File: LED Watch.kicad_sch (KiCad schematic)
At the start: 0 parts

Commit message: first schematic progress commit. adding RGB sketch schematic as well as completed single LED ring sketch. need to add buttons and sort out AND gates in the RGB sketch.
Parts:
- added D1, D10, D100, D101, D102, D103, D104, D105, D106, D107, D108, D109, D11, D110, D111, D112, D113, D114, D115, D116, D117, D118, D119, D12, D120, D121, D122, D123, D124, D125, D126, D127, D128, D129, D13, D130, D131, D132, D14, D15, D16, D17, D18, D19, D2, D20, D21, D22, D23, D24, D25, D26, D27, D28, D29, D3, D30, D31, D32, D33, D34, D35, D36, D37, D38, D39, D4, D40, D41, D42, D43, D44, D45, D46, D47, D48, D49, D5, D50, D51, D52, D53, D54, D55, D56, D57, D58, D59, D6, D60, D61, D62, D63, D64, D65, D66, D67, D68, D69, D7, D70, D71, D72, D73, D74, D75, D76, D77, D78, D79, D8, D80, D81, D82, D83, D84, D85, D86, D87, D88, D89, D9, D90, D91, D92, D93, D94, D95, D96, D97, D98, D99: LG_L29K-G2J1-24-Z, digikey-footprints:0603, symbol dk_LED-Indication-Discrete:LG_L29K-G2J1-24-Z
- added Q1, Q10, Q11, Q12, Q13, Q2, Q3, Q4, Q5, Q6, Q7, Q8, Q9: BD135, Package_TO_SOT_THT:TO-126-3_Vertical, symbol Transistor_BJT:BD135
- added R1, R10, R11, R12, R13, R14, R15, R16, R17, R18, R19, R2, R20, R21, R22, R23, R24, R25, R3, R4, R5, R6, R7, R8, R9: R_US, symbol Device:R_US
- added U1: ATMEGA32U4-AU, digikey-footprints:TQFP-44_10x10mm, symbol dk_Embedded-Microcontrollers:ATMEGA32U4-AU
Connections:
- new net: D51.2, D60.2, D61.1, D70.1, Q6.2 (C)
- new net: D61.2, D70.2, D71.1, D80.1, Q7.2 (C)
- new net: D32.2, D42.1
- new net: D42.2, D52.1
- new net: D121.2, D122.2, D123.2, D124.2, D125.2, D126.2, D127.2, D128.2, D129.2, D130.2, D131.2, D132.2, Q13.2 (C)
- new net: Q13.3 (B), R1.2
- new net: Q8.3 (B), R6.2
- new net: D1.2, D10.2, D11.1, D20.1, Q1.2 (C)
- new net: D11.2, D20.2, D21.1, D30.1, Q2.2 (C)
- new net: D18.1, D8.2
- new net: D18.2, D28.1
- new net: D41.2, D50.2, D51.1, D60.1, Q5.2 (C)
- new net: Q5.3 (B), R9.2
- new net: Q7.3 (B), R7.2
- new net: D109.1, D99.2
- new net: D109.2, D119.1
- new net: D105.1, D95.2
- new net: D105.2, D115.1
- new net: D100.1, D81.2, D90.2, D91.1, Q9.2 (C)
- new net: D100.2, D101.1, D110.1, D91.2, Q10.2 (C)
- new net: D83.2, D93.1
- new net: D103.1, D93.2
- new net: D112.2, D122.1
- new net: D117.2, D127.1
- new net: D9.1, R22.2
- new net: D74.2, D84.1
- new net: D84.2, D94.1
- new net: D103.2, D113.1
- new net: D113.2, D123.1
- new net: D21.2, D30.2, D31.1, D40.1, Q3.2 (C)
- new net: D53.2, D63.1
- new net: D63.2, D73.1
- new net: D10.1, R23.2
- new net: D31.2, D40.2, D41.1, D50.1, Q4.2 (C)
- new net: D16.1, D6.2
- new net: D16.2, D26.1
- new net: D78.2, D88.1
- new net: D88.2, D98.1
- new net: D108.2, D118.1
- new net: D118.2, D128.1
- new net: D37.2, D47.1
- new net: D47.2, D57.1
- new net: D14.1, D4.2
- new net: D14.2, D24.1
- new net: D102.1, D92.2
- new net: D102.2, D112.1
- new net: D71.2, D80.2, D81.1, D90.1, Q8.2 (C)
- new net: D39.2, D49.1
- new net: D49.2, D59.1
- new net: D15.1, D5.2
- new net: D15.2, D25.1
- new net: D54.2, D64.1
- new net: D64.2, D74.1
- new net: D116.2, D126.1
- new net: D17.1, D7.2
- new net: D17.2, D27.1
- new net: D48.2, D58.1
- new net: D58.2, D68.1
- new net: D5.1, R18.2
- new net: Q2.3 (B), R12.2
- new net: Q3.3 (B), R11.2
- new net: D19.1, D9.2
- new net: D19.2, D29.1
- new net: D67.2, D77.1
- new net: D77.2, D87.1
- new net: D132.1, D7.1, R20.2, R25.2
- new net: D27.2, D37.1
- new net: D8.1, R21.2
- new net: D57.2, D67.1
- new net: D101.2, D110.2, D111.1, D120.1, Q11.2 (C)
- new net: Q11.3 (B), R3.2
- new net: D2.1, R15.2
- new net: D12.1, D2.2
- new net: D87.2, D97.1
- new net: D107.1, D97.2
- new net: D29.2, D39.1
- new net: D62.2, D72.1
- new net: D72.2, D82.1
- new net: D66.2, D76.1
- new net: D76.2, D86.1
- new net: D69.2, D79.1
- new net: D79.2, D89.1
- new net: D131.1, D6.1, R19.2, R24.2
- new net: D86.2, D96.1
- new net: D106.2, D116.1
- new net: Q6.3 (B), R8.2
- new net: D65.2, D75.1
- new net: D75.2, D85.1
- new net: D46.2, D56.1
- new net: D56.2, D66.1
- new net: D45.2, D55.1
- new net: D55.2, D65.1
- new net: Q9.3 (B), R5.2
- new net: D107.2, D117.1
- new net: D52.2, D62.1
- new net: D4.1, R17.2
- new net: D111.2, D120.2, D121.1, D130.1, Q12.2 (C)
- new net: D119.2, D129.1
- new net: D13.1, D3.2
- new net: D13.2, D23.1
- new net: Q1.3 (B), R13.2
- new net: Q10.3 (B), R4.2
- new net: Q4.3 (B), R10.2
- new net: Q12.3 (B), R2.2
- new net: D89.2, D99.1
- new net: D22.2, D32.1
- new net: D114.2, D124.1
- new net: D25.2, D35.1
- new net: D108.1, D98.2
- new net: D34.2, D44.1
- new net: D44.2, D54.1
- new net: D68.2, D78.1
- new net: D106.1, D96.2
- new net: D23.2, D33.1
- new net: D33.2, D43.1
- new net: D85.2, D95.1
- new net: D12.2, D22.1
- new net: D73.2, D83.1
- new net: D59.2, D69.1
- new net: D82.2, D92.1
- new net: D115.2, D125.1
- new net: D1.1, R14.2
- new net: D3.1, R16.2
- new net: D104.1, D94.2
- new net: D104.2, D114.1
- new net: D26.2, D36.1
- new net: D36.2, D46.1
- new net: D35.2, D45.1
- new net: D28.2, D38.1
- new net: D38.2, D48.1
- new net: D43.2, D53.1
- new net: D24.2, D34.1
- new net GND: Q1.1 (E), Q10.1 (E), Q11.1 (E), Q12.1 (E), Q13.1 (E), Q2.1 (E), Q3.1 (E), Q4.1 (E), Q5.1 (E), Q6.1 (E), Q7.1 (E), Q8.1 (E), Q9.1 (E)

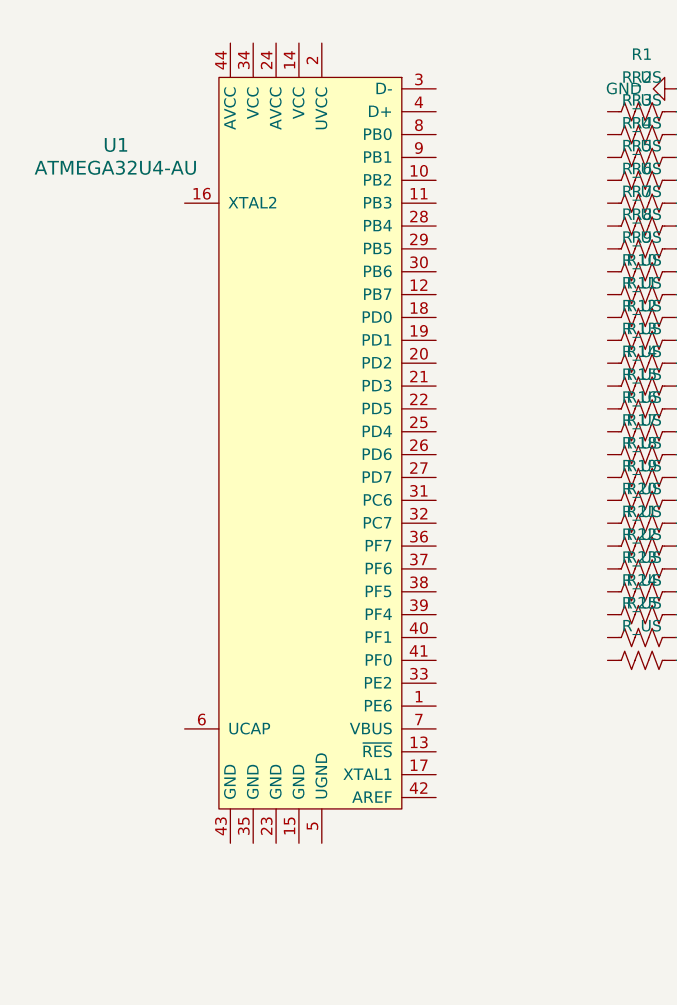
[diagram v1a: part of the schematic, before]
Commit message: chip swap to atmega4808
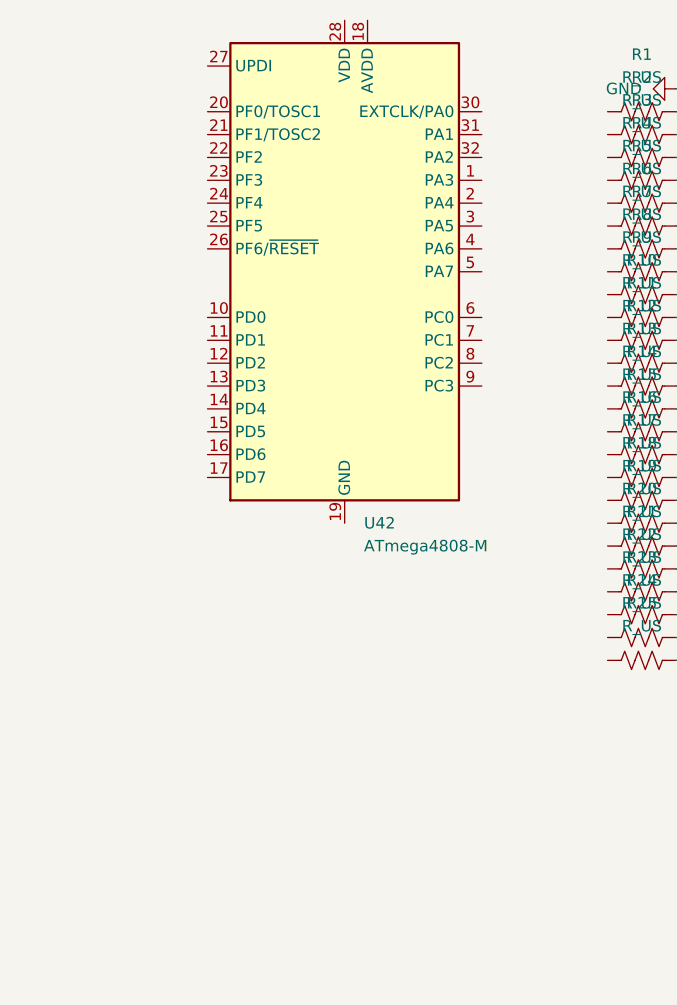
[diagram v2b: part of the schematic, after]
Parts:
- removed U1: ATMEGA32U4-AU, digikey-footprints:TQFP-44_10x10mm, symbol dk_Embedded-Microcontrollers:ATMEGA32U4-AU
- added U42: ATmega4808-M, Package_DFN_QFN:QFN-32-1EP_5x5mm_P0.5mm_EP3.1x3.1mm_ThermalVias, symbol MCU_Microchip_ATmega:ATmega4808-M
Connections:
- new net: U42.19 (GND), U42.29 (GND), U42.33 (GND)
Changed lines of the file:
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@@
 	)
 	(symbol
-		(lib_id "dk_Embedded-Microcontrollers:ATMEGA32U4-AU")
-		(at 110.49 102.87 0)
-		(mirror y)
-		(unit 1)
-		(exclude_from_sim no)
-		(in_bom yes)
-		(on_board yes)
-		(dnp no)
-		(property "Reference" "U1"
-			(at 90.17 76.1298 0)
-			(effects
-				(font
-					(size 1.524 1.524)
-				)
-			)
-		)
-		(property "Value" "ATMEGA32U4-AU"
-			(at 90.17 78.6698 0)
-			(effects
-				(font
-					(size 1.524 1.524)
-				)
-			)
-		)
-		(property "Footprint" "digikey-footprints:TQFP-44_10x10mm"
-			(at 105.41 97.79 0)
-			(effects
-				(font
-					(size 1.524 1.524)
-				)
-				(justify left)
-				(hide yes)
-			)
-		)
-		(property "Datasheet" "http://ww1.microchip.com/downloads/en/DeviceDoc/Atmel-7766-8-bit-AVR-ATmega16U4-32U4_Summary.pdf"
-			(at 105.41 95.25 0)
-			(effects
-				(font
-					(size 1.524 1.524)
-				)
-				(justify left)
-				(hide yes)
-			)
-		)
-		(property "Description" "IC MCU 8BIT 32KB FLASH 44TQFP"
-			(at 110.49 102.87 0)
-			(effects
-				(font
-					(size 1.27 1.27)
-				)
-				(hide yes)
-			)
-		)
-		(property "Digi-Key_PN" "ATMEGA32U4-AU-ND"
-			(at 105.41 92.71 0)
-			(effects
-				(font
-					(size 1.524 1.524)
-				)
-				(justify left)
-				(hide yes)
-			)
-		)
-		(property "MPN" "ATMEGA32U4-AU"
-			(at 105.41 90.17 0)
-			(effects
-				(font
-					(size 1.524 1.524)
-				)
-				(justify left)
-				(hide yes)
-			)
-		)
-		(property "Category" "Integrated Circuits (ICs)"
-			(at 105.41 87.63 0)
-			(effects
-				(font
-					(size 1.524 1.524)
-				)
-				(justify left)
-				(hide yes)
-			)
-		)
-		(property "Family" "Embedded - Microcontrollers"
-			(at 105.41 85.09 0)
-			(effects
-				(font
-					(size 1.524 1.524)
-				)
-				(justify left)
-				(hide yes)
-			)
-		)
-		(property "DK_Datasheet_Link" "http://ww1.microchip.com/downloads/en/DeviceDoc/Atmel-7766-8-bit-AVR-ATmega16U4-32U4_Summary.pdf"
-			(at 105.41 82.55 0)
-			(effects
-				(font
-					(size 1.524 1.524)
-				)
-				(justify left)
-				(hide yes)
-			)
-		)
-		(property "DK_Detail_Page" "/product-detail/en/microchip-technology/ATMEGA32U4-AU/ATMEGA32U4-AU-ND/1914602"
-			(at 105.41 80.01 0)
-			(effects
-				(font
-					(size 1.524 1.524)
-				)
-				(justify left)
-				(hide yes)
-			)
-		)
-		(property "Description_1" "IC MCU 8BIT 32KB FLASH 44TQFP"
-			(at 105.41 77.47 0)
-			(effects
-				(font
-					(size 1.524 1.524)
-				)
-				(justify left)
-				(hide yes)
-			)
-		)
-		(property "Manufacturer" "Microchip Technology"
-			(at 105.41 74.93 0)
-			(effects
-				(font
-					(size 1.524 1.524)
-				)
-				(justify left)
-				(hide yes)
-			)
-		)
-		(property "Status" "Active"
-			(at 105.41 72.39 0)
-			(effects
-				(font
-					(size 1.524 1.524)
-				)
-				(justify left)
-				(hide yes)
-			)
-		)
-		(pin "18"
-		)
-		(pin "3"
-		)
-		(pin "11"
-		)
-		(pin "8"
-		)
-		(pin "28"
-		)
-		(pin "4"
-		)
-		(pin "29"
-		)
-		(pin "30"
-		)
-		(pin "9"
-		)
-		(pin "10"
-		)
-		(pin "12"
-		)
-		(pin "41"
-		)
-		(pin "13"
-		)
-		(pin "26"
-		)
-		(pin "36"
-		)
-		(pin "22"
-		)
-		(pin "31"
-		)
-		(pin "19"
-		)
-		(pin "21"
-		)
-		(pin "20"
-		)
-		(pin "27"
-		)
-		(pin "32"
-		)
-		(pin "38"
-		)
-		(pin "40"
-		)
-		(pin "7"
-		)
-		(pin "24"
-		)
-		(pin "39"
-		)
-		(pin "14"
-		)
-		(pin "5"
-		)
-		(pin "25"
-		)
-		(pin "37"
-		)
-		(pin "33"
-		)
-		(pin "1"
-		)
-		(pin "42"
-		)
-		(pin "44"
-		)
-		(pin "35"
-		)
-		(pin "2"
-		)
-		(pin "43"
-		)
-		(pin "23"
-		)
-		(pin "16"
-		)
-		(pin "15"
-		)
-		(pin "17"
-		)
-		(pin "34"
-		)
-		(pin "6"
-		)
-		(instances
-			(project ""
-				(path "/4f6e3ccb-61a7-41db-9176-b9c2e62eec38"
-					(reference "U1")
-					(unit 1)
-				)
-			)
-		)
-	)
-	(symbol
 		(lib_id "Device:R_US")
 		(at 148.59 107.95 90)
@@
 					(unit 1)
 				)
+			)
+		)
+	)
+	(symbol
+		(lib_id "MCU_Microchip_ATmega:ATmega4808-M")
+		(at 115.57 90.17 0)
+		(unit 1)
+		(exclude_from_sim no)
+		(in_bom yes)
+		(on_board yes)
+		(dnp no)
+		(fields_autoplaced yes)
+		(property "Reference" "U42"
+			(at 117.7133 118.11 0)
+			(effects
+				(font
+					(size 1.27 1.27)
+				)
+				(justify left)
+			)
+		)
+		(property "Value" "ATmega4808-M"
+			(at 117.7133 120.65 0)
+			(effects
+				(font
+					(size 1.27 1.27)
+				)
+				(justify left)
+			)
+		)
+		(property "Footprint" "Package_DFN_QFN:QFN-32-1EP_5x5mm_P0.5mm_EP3.1x3.1mm_ThermalVias"
+			(at 115.57 90.17 0)
+			(effects
+				(font
+					(size 1.27 1.27)
+					(italic yes)
+				)
+				(hide yes)
+			)
+		)
+		(property "Datasheet" "http://ww1.microchip.com/downloads/en/DeviceDoc/40002017A.pdf"
+			(at 115.57 90.17 0)
+			(effects
+				(font
+					(size 1.27 1.27)
+				)
+				(hide yes)
+			)
+		)
+		(property "Description" "20MHz, 48kB Flash, 6kB SRAM, 256B EEPROM, VQFN-32"
+			(at 115.57 90.17 0)
+			(effects
+				(font
+					(size 1.27 1.27)
+				)
+				(hide yes)
+			)
+		)
+		(pin "28"
+		)
+		(pin "10"
+		)
+		(pin "15"
+		)
+		(pin "23"
+		)
+		(pin "17"
+		)
+		(pin "27"
+		)
+		(pin "26"
+		)
+		(pin "11"
+		)
+		(pin "16"
+		)
+		(pin "21"
+		)
+		(pin "25"
+		)
+		(pin "13"
+		)
+		(pin "12"
+		)
+		(pin "4"
+		)
+		(pin "22"
+		)
+		(pin "24"
+		)
+		(pin "20"
+		)
+		(pin "14"
+		)
+		(pin "18"
+		)
+		(pin "5"
+		)
+		(pin "30"
+		)
+		(pin "19"
+		)
+		(pin "31"
+		)
+		(pin "32"
+		)
+		(pin "1"
+		)
+		(pin "6"
+		)
+		(pin "33"
+		)
+		(pin "3"
+		)
+		(pin "8"
+		)
+		(pin "7"
+		)
+		(pin "29"
+		)
+		(pin "2"
+		)
+		(pin "9"
+		)
+		(instances
+			(project "LED Watch"
+				(path "/4f6e3ccb-61a7-41db-9176-b9c2e62eec38"
+					(reference "U42")
+					(unit 1)
+				)
